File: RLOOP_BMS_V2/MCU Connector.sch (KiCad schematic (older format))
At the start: 2 parts, among them J1 1241050-7, J3 TE 2-292161-3

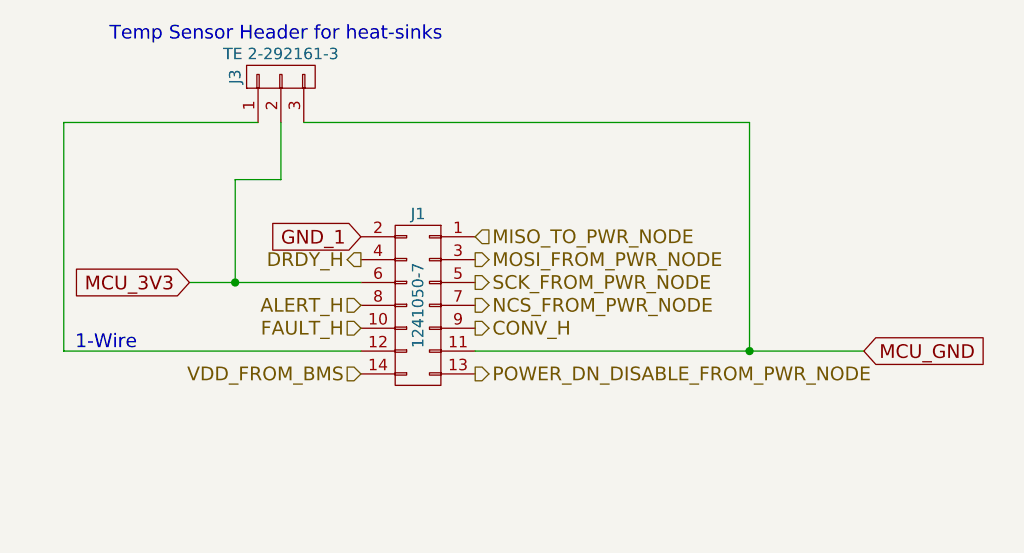
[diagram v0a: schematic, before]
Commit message: swapped a few connectors to standardize with the power node and what's readily available
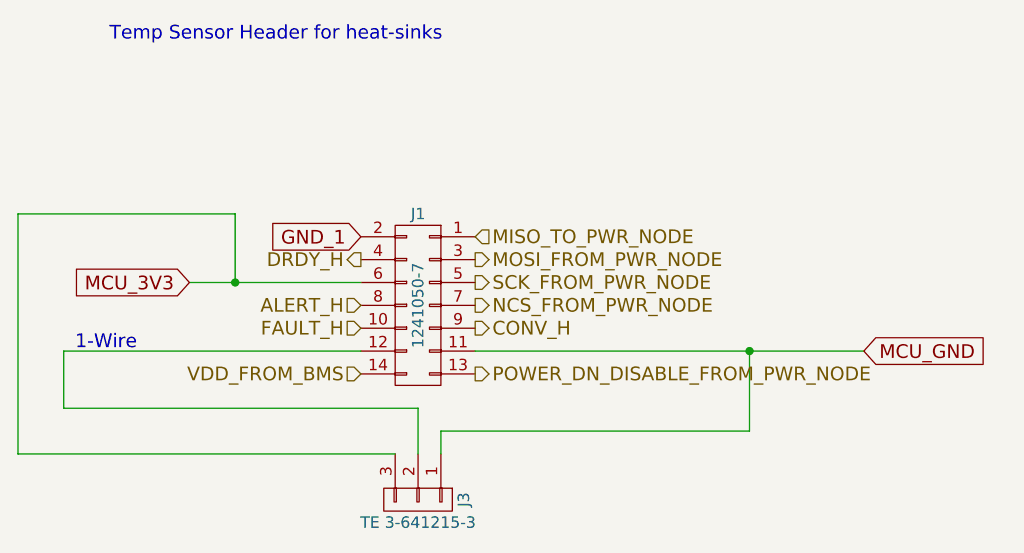
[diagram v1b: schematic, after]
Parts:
- J3: value TE 2-292161-3 -> TE 3-641215-3; footprint Pin_Headers:Pin_Header_Straight_1x03_Pitch2.00mm -> rLoop_Footprints:3-641215-3_3Pin_Latching_Header
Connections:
- net MCU_3V3: now also J3.3 (P3); no longer J3.2 (P2)
- net MCU_GND: now also J3.1 (P1); no longer J3.3 (P3)
- net at J1.12 (P12): now also J3.2 (P2); no longer J3.1 (P1)
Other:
- moved on the sheet: J3
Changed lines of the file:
@@
 DRDY_H
 Wire Wire Line
-	3300 3700 3300 2700
-Wire Wire Line
-	3300 2700 4150 2700
-Wire Wire Line
-	6800 3700 5100 3700
+	5100 3700 6800 3700
 Wire Wire Line
 	3850 3400 4600 3400
@@
 L CONN_01X03 J3
 U 1 1 594AAEB6
-P 4250 2500
-F 0 "J3" H 4250 2700 50  0000 C CNN
-F 1 "TE 2-292161-3" V 4350 2500 50  0000 C CNN
-F 2 "Pin_Headers:Pin_Header_Straight_1x03_Pitch2.00mm" H 4250 2500 50  0001 C CNN
-F 3 "" H 4250 2500 50  0001 C CNN
-	1    4250 2500
-	0    -1   -1   0
+P 4850 4350
+F 0 "J3" H 4850 4550 50  0000 C CNN
+F 1 "TE 3-641215-3" V 4950 4350 50  0000 C CNN
+F 2 "rLoop_Footprints:3-641215-3_3Pin_Latching_Header" H 4850 4350 50  0001 C CNN
+F 3 "" H 4850 4350 50  0001 C CNN
+	1    4850 4350
+	0    1    1    0
 $EndComp
-Wire Wire Line
-	4250 2700 4250 2950
-Wire Wire Line
-	4250 2950 4050 2950
-Wire Wire Line
-	4050 2950 4050 3400
 Connection ~ 4050 3400
 Wire Wire Line
-	4350 2700 6300 2700
-Wire Wire Line
-	6300 2700 6300 3700
+	6300 3700 6300 4050
 Connection ~ 6300 3700
 Text Notes 3350 3700 0    60   ~ 0
@@
 Text Notes 3500 2350 0    60   ~ 0
 Temp Sensor Header for heat-sinks
+Wire Wire Line
+	6300 4050 4950 4050
+Wire Wire Line
+	4950 4050 4950 4150
+Wire Wire Line
+	3300 3700 3300 3950
+Wire Wire Line
+	3300 3950 4850 3950
+Wire Wire Line
+	4850 3950 4850 4150
+Wire Wire Line
+	4050 3400 4050 3100
+Wire Wire Line
+	4050 3100 3100 3100
+Wire Wire Line
+	3100 3100 3100 4150
+Wire Wire Line
+	3100 4150 4750 4150
 $EndSCHEMATC
